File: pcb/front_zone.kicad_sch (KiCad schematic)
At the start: 0 parts

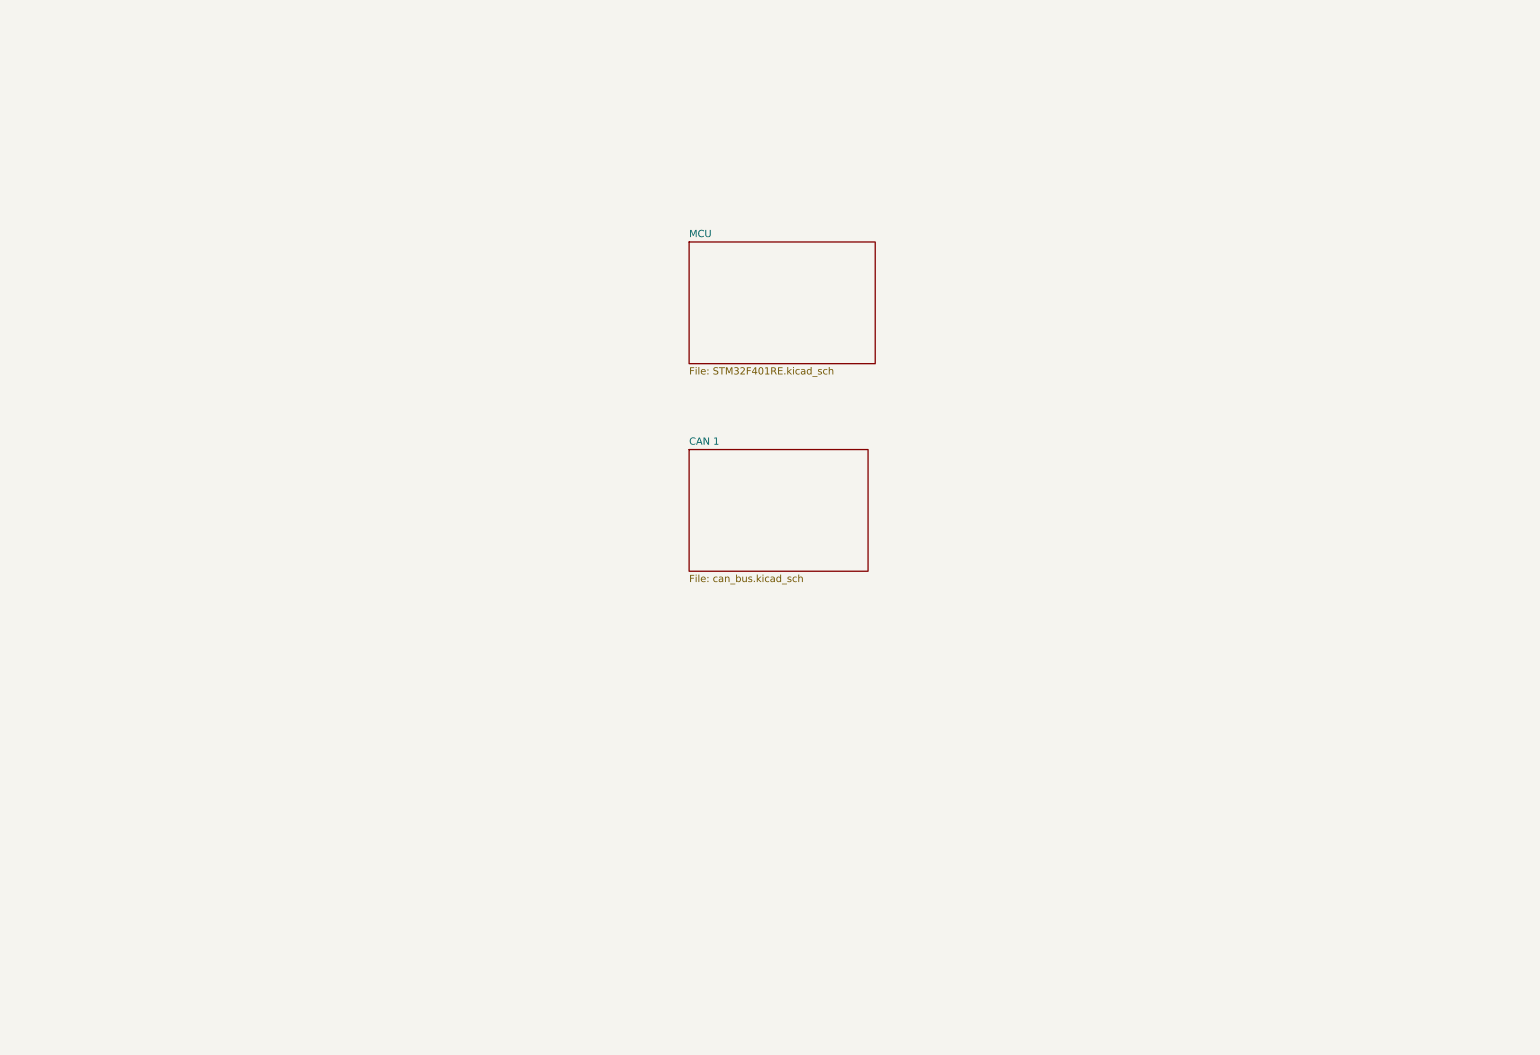
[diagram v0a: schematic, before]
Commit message: Added Front and Rear zone sheets made of CAN and MCU design sheets.
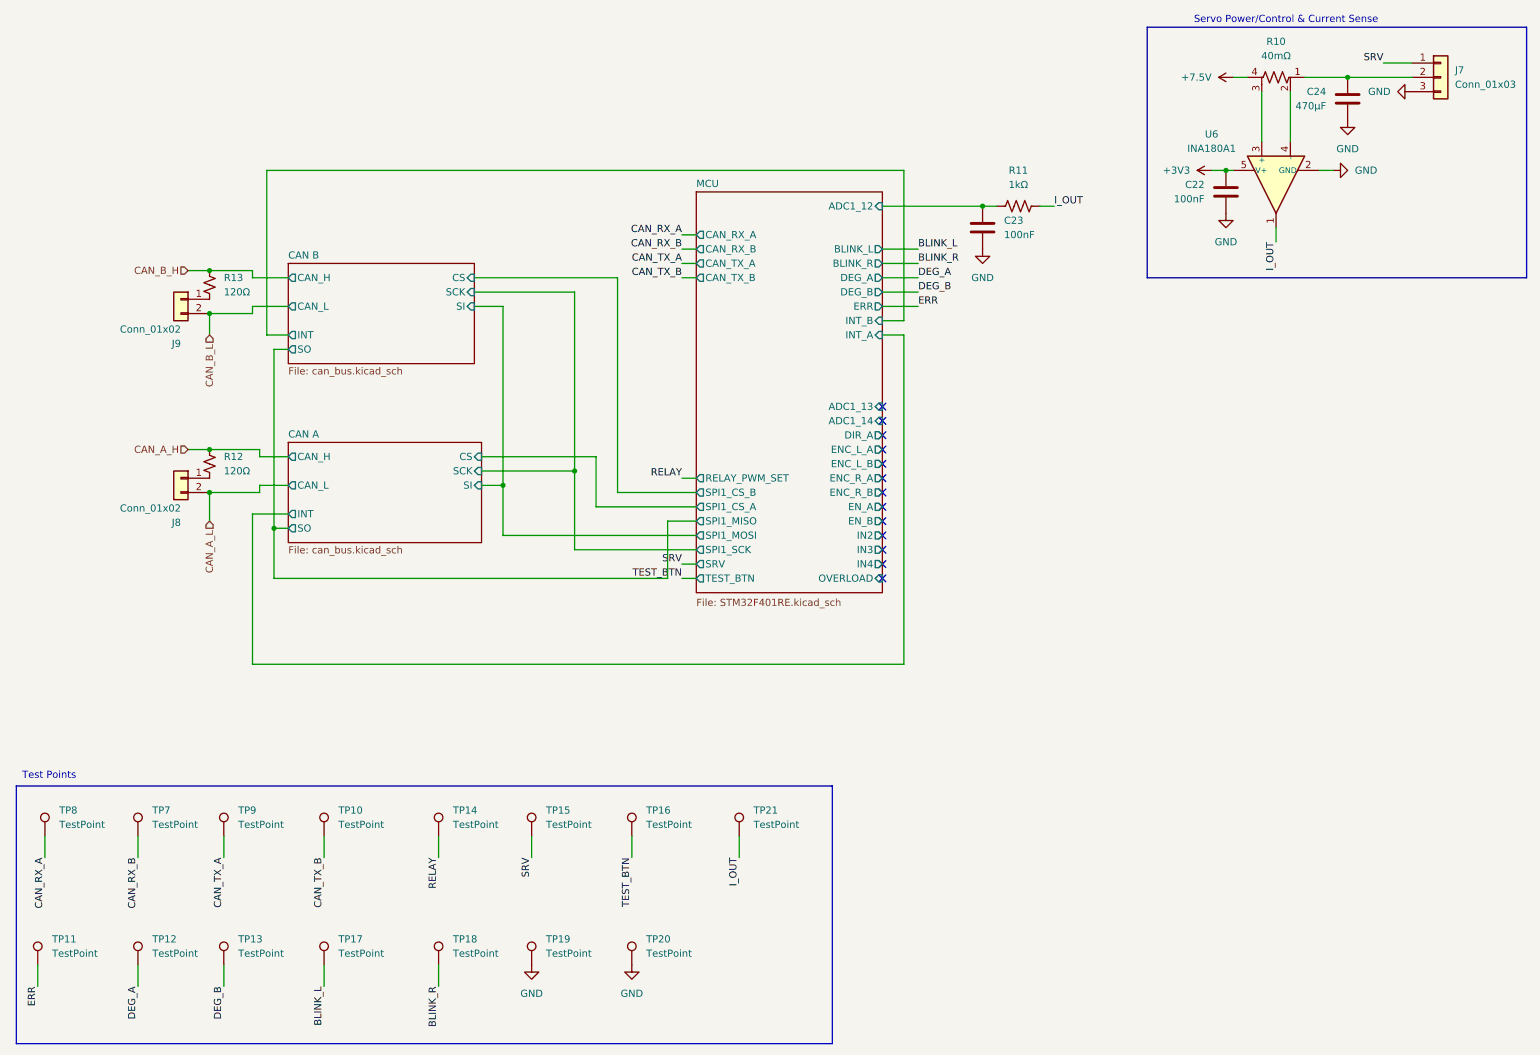
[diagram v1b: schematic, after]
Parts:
- added C22, C23: 100nF, symbol Device:C
- added C24: 470μF, symbol Device:C
- added J7: Conn_01x03, symbol Connector_Generic:Conn_01x03
- added J8, J9: Conn_01x02, symbol Connector_Generic:Conn_01x02
- added R10: 40mΩ, symbol Device:R_Shunt_US
- added R11: 1kΩ, symbol Device:R_US
- added R12, R13: 120Ω, symbol Device:R_Small_US
- added TP10, TP11, TP12, TP13, TP14, TP15, TP16, TP17, TP18, TP19, TP20, TP21, TP7, TP8, TP9: TestPoint, symbol Connector:TestPoint
- added U6: INA180A1, Package_TO_SOT_SMD:SOT-23-5, symbol Amplifier_Current:INA180A1
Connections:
- new net: J9.1 (Pin_1), R13.2
- new net: C24.1, J7.2 (Pin_2), R10.1
- new net: R10.3, U6.3 (+)
- new net: R10.2, U6.4 (-)
- new net: J8.1 (Pin_1), R12.2
- new net +3V3: C22.1, U6.5 (V+)
- new net +7.5V: R10.4
- new net BLINK_L: TP17.1
- new net BLINK_R: TP18.1
- new net CAN_A_H: R12.1
- new net CAN_A_L: J8.2 (Pin_2)
- new net CAN_B_H: R13.1
- new net CAN_B_L: J9.2 (Pin_2)
- new net CAN_RX_A: TP8.1
- new net CAN_RX_B: TP7.1
- new net CAN_TX_A: TP9.1
- new net CAN_TX_B: TP10.1
- new net DEG_A: TP12.1
- new net DEG_B: TP13.1
- new net ERR: TP11.1
- new net GND: C22.2, C23.2, C24.2, J7.3 (Pin_3), TP19.1, TP20.1, U6.2 (GND)
- new net I_OUT: R11.2, TP21.1, U6.1
- new net MCU/ADC1_12: C23.1, R11.1
- new net RELAY: TP14.1
- new net SRV: J7.1 (Pin_1), TP15.1
- new net TEST_BTN: TP16.1
- no-connect marks 0 -> 13
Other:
- removed sheet CAN 1
- added sheet CAN A (can_bus.kicad_sch)
- added sheet CAN B (can_bus.kicad_sch)
- sheet MCU ports: added ADC1_12, ADC1_13, ADC1_14, BLINK_L, BLINK_R, CAN_RX_A, CAN_RX_B, CAN_TX_A, CAN_TX_B, DEG_A, DEG_B, DIR_A, ENC_L_A, ENC_L_B, ENC_R_A, ENC_R_B, EN_A, EN_B, ERR, IN2, IN3, IN4, INT_A, INT_B, OVERLOAD, RELAY_PWM_SET, SPI1_CS_A, SPI1_CS_B, SPI1_MISO, SPI1_MOSI, SPI1_SCK, SRV, TEST_BTN; removed none
- note added: "Servo Power/Control & Current Sense"
- note added: "Test Points"

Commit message: Added footprints to all components.
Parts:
- C201: renamed from C23; footprint (none) -> Capacitor_SMD:C_0603_1608Metric
- C202: renamed from C22; footprint (none) -> Capacitor_SMD:C_0603_1608Metric
- C203: renamed from C24; footprint (none) -> Capacitor_SMD:CP_Elec_8x11.9
- J201: renamed from J9; footprint (none) -> Connector_PinHeader_2.54mm:PinHeader_1x02_P2.54mm_Vertical
- J202: renamed from J8; footprint (none) -> Connector_PinHeader_2.54mm:PinHeader_1x02_P2.54mm_Vertical
- J203: renamed from J7; footprint (none) -> Connector_PinHeader_2.54mm:PinHeader_1x03_P2.54mm_Vertical
- R201: renamed from R13; footprint (none) -> Resistor_SMD:R_0603_1608Metric
- R202: renamed from R12; footprint (none) -> Resistor_SMD:R_0603_1608Metric
- R203: renamed from R11; footprint (none) -> Resistor_SMD:R_0603_1608Metric
- R204: renamed from R10; footprint (none) -> Resistor_SMD:R_2512_6332Metric; symbol Device:R_Shunt_US -> Device:R
- TP201: renamed from TP11; footprint (none) -> TestPoint:TestPoint_Keystone_5015_Micro_Mini
- TP202: renamed from TP8; footprint (none) -> TestPoint:TestPoint_Keystone_5015_Micro_Mini
- TP203: renamed from TP7; footprint (none) -> TestPoint:TestPoint_Keystone_5015_Micro_Mini
- TP204: renamed from TP12; footprint (none) -> TestPoint:TestPoint_Keystone_5015_Micro_Mini
- TP205: renamed from TP9; footprint (none) -> TestPoint:TestPoint_Keystone_5015_Micro_Mini
- TP206: renamed from TP13; footprint (none) -> TestPoint:TestPoint_Keystone_5015_Micro_Mini
- TP207: renamed from TP10; footprint (none) -> TestPoint:TestPoint_Keystone_5015_Micro_Mini
- TP208: renamed from TP17; footprint (none) -> TestPoint:TestPoint_Keystone_5015_Micro_Mini
- TP209: renamed from TP14; footprint (none) -> TestPoint:TestPoint_Keystone_5015_Micro_Mini
- TP210: renamed from TP18; footprint (none) -> TestPoint:TestPoint_Keystone_5015_Micro_Mini
- TP211: renamed from TP15; footprint (none) -> TestPoint:TestPoint_Keystone_5015_Micro_Mini
- TP212: renamed from TP19; footprint (none) -> TestPoint:TestPoint_Keystone_5015_Micro_Mini
- TP213: renamed from TP16; footprint (none) -> TestPoint:TestPoint_Keystone_5015_Micro_Mini
- TP214: renamed from TP20; footprint (none) -> TestPoint:TestPoint_Keystone_5015_Micro_Mini
- TP215: renamed from TP21; footprint (none) -> TestPoint:TestPoint_Keystone_5015_Micro_Mini
- renumbered U6 to U201
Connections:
- net +7.5V: now also R204.2, U201.3 (+); no longer R204.4
- net at C203.1, J203.2 (Pin_2), R204.1: now also U201.4 (-)

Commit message: Added CAN Bus connectors and finalized schematic with BOM, LCSC #s, and links to parts.
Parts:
- C201, C202: LCSC (none) -> C18522636; MPN (none) -> KGM15AR71C104KT; Manufacturer (none) -> KYOCERA AVX
- C203: footprint Capacitor_SMD:CP_Elec_8x11.9 -> Capacitor_SMD:CP_Elec_10x12.6; LCSC (none) -> C1517666; MPN (none) -> A768MS477M1ELAE017; Manufacturer (none) -> KEMET
- J201, J202: LCSC (none) -> C492401; MPN (none) -> PZ254V-11-02P
- J203: LCSC (none) -> C2937625; MPN (none) -> PZ254V-11-03P
- R201, R202: LCSC (none) -> C114640; MPN (none) -> RC0603FR-07120RL; Manufacturer (none) -> YAGEO
- R203: LCSC (none) -> C118155; MPN (none) -> ERJ-3EKF1001V; Manufacturer (none) -> Panasonic
- R204: LCSC (none) -> C844291; MPN (none) -> WSL2512R0400FEA; Manufacturer (none) -> Vishay Dale
- TP201, TP202, TP203, TP204, TP205, TP206, TP207, TP208, TP209, TP210, TP211, TP212, TP213, TP214, TP215: LCSC (none) -> C2906768; MPN (none) -> 5015; Manufacturer (none) -> Keystone Electronics
- U201: LCSC (none) -> C122228; MPN (none) -> INA180A1IDBVR; Manufacturer (none) -> Texas Instruments
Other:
- company: (none) -> 18-649 Lab 4: Controller PCB
- title: (none) -> Front Zone: Steering
